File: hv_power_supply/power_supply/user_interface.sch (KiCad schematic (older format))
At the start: 28 parts, among them SW1? EMS22A50-B28-LS6

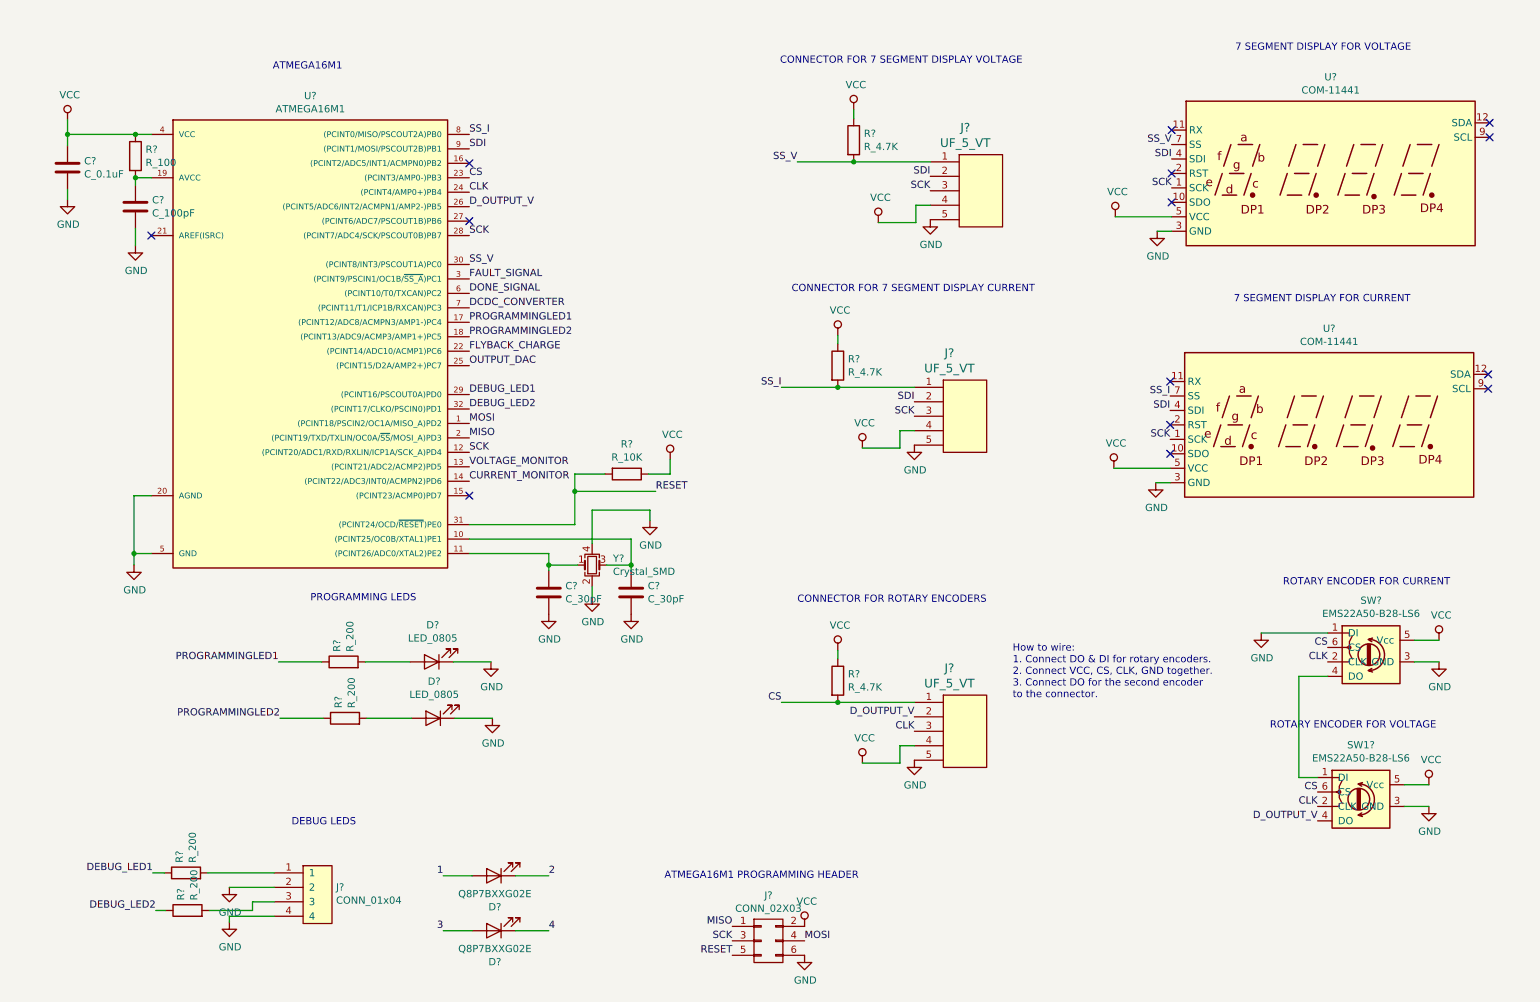
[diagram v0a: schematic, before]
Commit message: make schematic sheets talk to each other
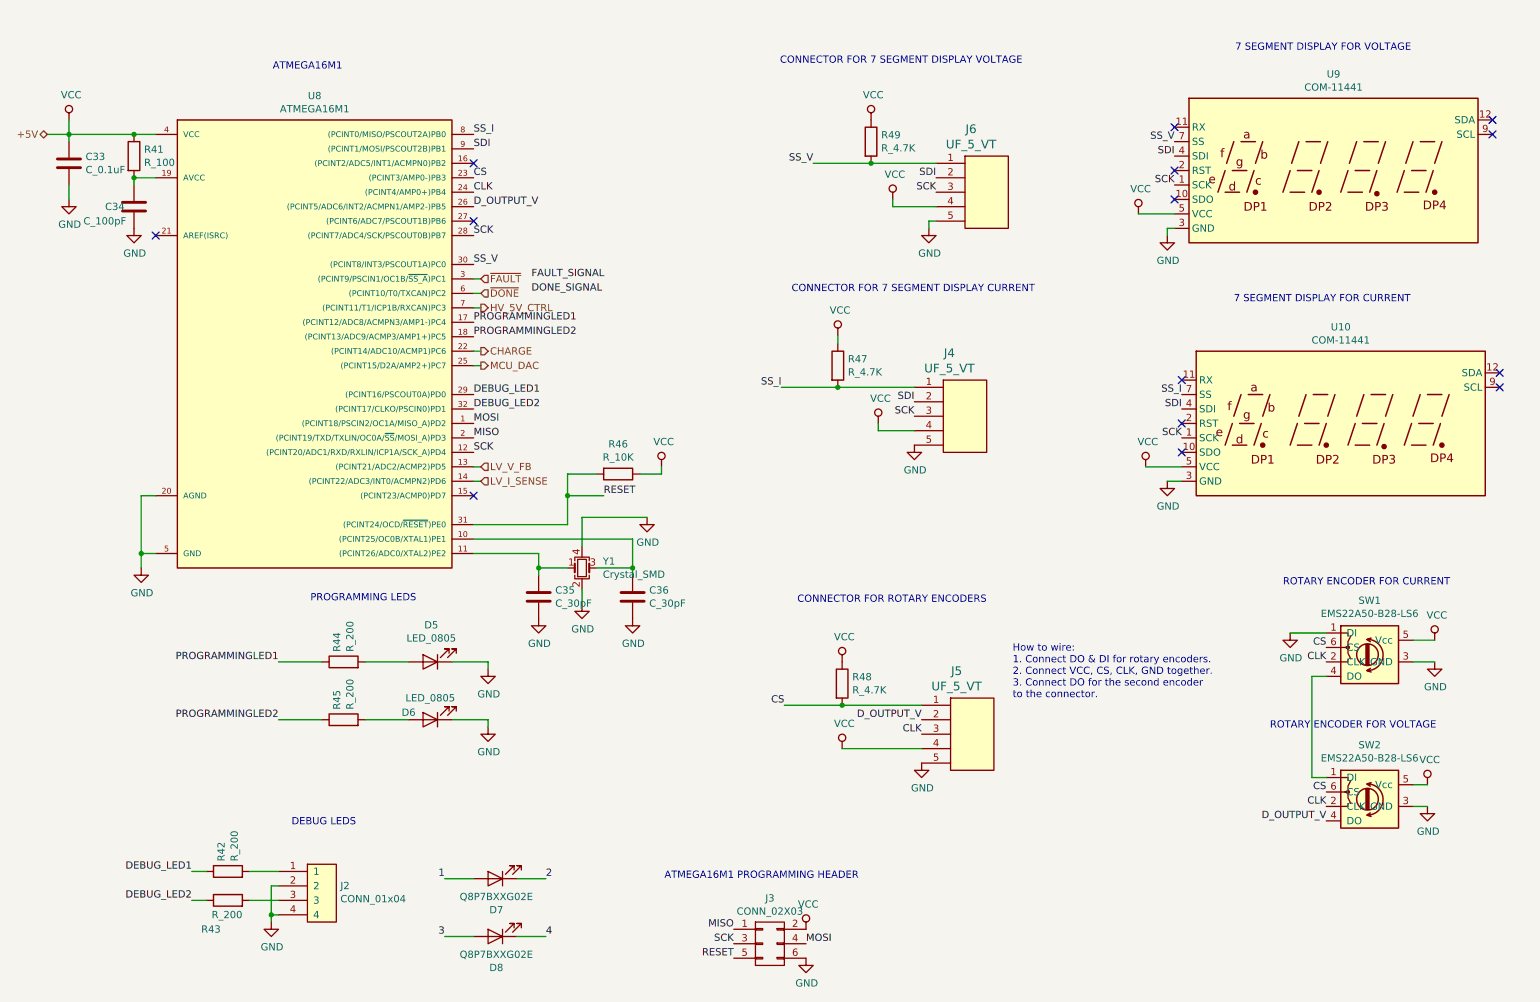
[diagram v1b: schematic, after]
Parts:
- gave numbers to parts that had none: 28
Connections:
- net DONE_SIGNAL: no longer U8.6 ((PCINT10/T0/TXCAN)PC2)
- net FAULT_SIGNAL: no longer U8.3 ((PCINT9/PSCIN1/OC1B/~SS_A~)PC1)
- net CURRENT_MONITOR renamed LV_I_SENSE
- net DCDC_CONVERTER renamed HV_5V_CTRL
- net FLYBACK_CHARGE renamed CHARGE
- net OUTPUT_DAC renamed MCU_DAC
- net VOLTAGE_MONITOR renamed LV_V_FB
- new net ~DONE: U8.6 ((PCINT10/T0/TXCAN)PC2)
- new net ~FAULT: U8.3 ((PCINT9/PSCIN1/OC1B/~SS_A~)PC1)
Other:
- moved on the sheet: C33, C35, C36, D6, D7, D8, J2, J3, J5, J6, R42, R43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

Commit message: removed footprints from off-board components
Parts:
- D7, D8: footprint footprints:LED_0805_OEM -> (none)
- U10, U9: footprint Display_7Segment:CA56-12EWA -> (none)
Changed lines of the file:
@@
 F 0 "U9" H 9650 2417 50  0000 C CNN
 F 1 "COM-11441" H 9650 2326 50  0000 C CNN
-F 2 "Display_7Segment:CA56-12EWA" H 9650 1150 50  0001 C CNN
+F 2 "" H 9650 1150 50  0001 C CNN
 F 3 "https://github.com/sparkfun/Serial7SegmentDisplay/wiki/Serial-7-Segment-Display-Datasheet" H 9220 1780 50  0001 C CNN
 	1    9650 1750
@@
 F 0 "D7" H 3843 6866 50  0000 C CNN
 F 1 "Q8P7BXXG02E" H 3843 6775 50  0000 C CNN
-F 2 "footprints:LED_0805_OEM" H 3750 6650 50  0001 C CNN
+F 2 "" H 3750 6650 50  0001 C CNN
 F 3 "https://www.apem.com/us/index.php?controller=attachment&id_attachment=1780" H 3850 6750 50  0001 C CNN
 F 4 "DK" H 3850 6650 60  0001 C CNN "MFN"
@@
 F 0 "D8" H 3843 7266 50  0000 C CNN
 F 1 "Q8P7BXXG02E" H 3843 7175 50  0000 C CNN
-F 2 "footprints:LED_0805_OEM" H 3750 7050 50  0001 C CNN
+F 2 "" H 3750 7050 50  0001 C CNN
 F 3 "https://www.apem.com/us/index.php?controller=attachment&id_attachment=1780" H 3850 7150 50  0001 C CNN
 F 4 "DK" H 3850 7050 60  0001 C CNN "MFN"
@@
 F 0 "U10" H 9700 4167 50  0000 C CNN
 F 1 "COM-11441" H 9700 4076 50  0000 C CNN
-F 2 "Display_7Segment:CA56-12EWA" H 9700 2900 50  0001 C CNN
+F 2 "" H 9700 2900 50  0001 C CNN
 F 3 "https://github.com/sparkfun/Serial7SegmentDisplay/wiki/Serial-7-Segment-Display-Datasheet" H 9270 3530 50  0001 C CNN
 	1    9700 3500

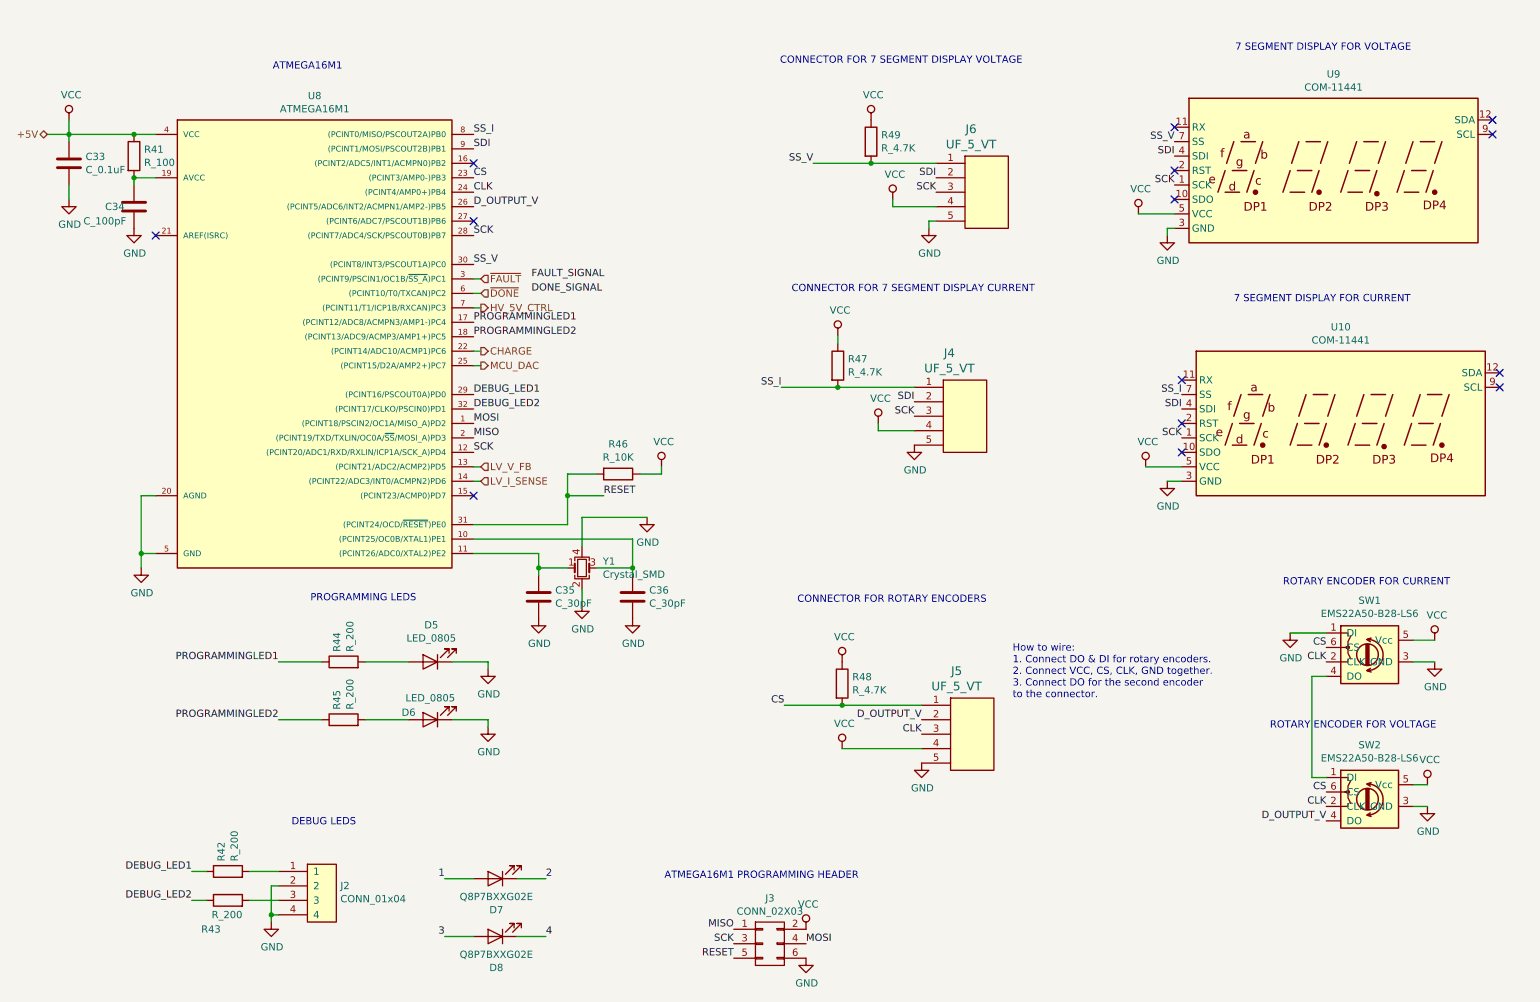
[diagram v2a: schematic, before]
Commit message: updated MCU pins
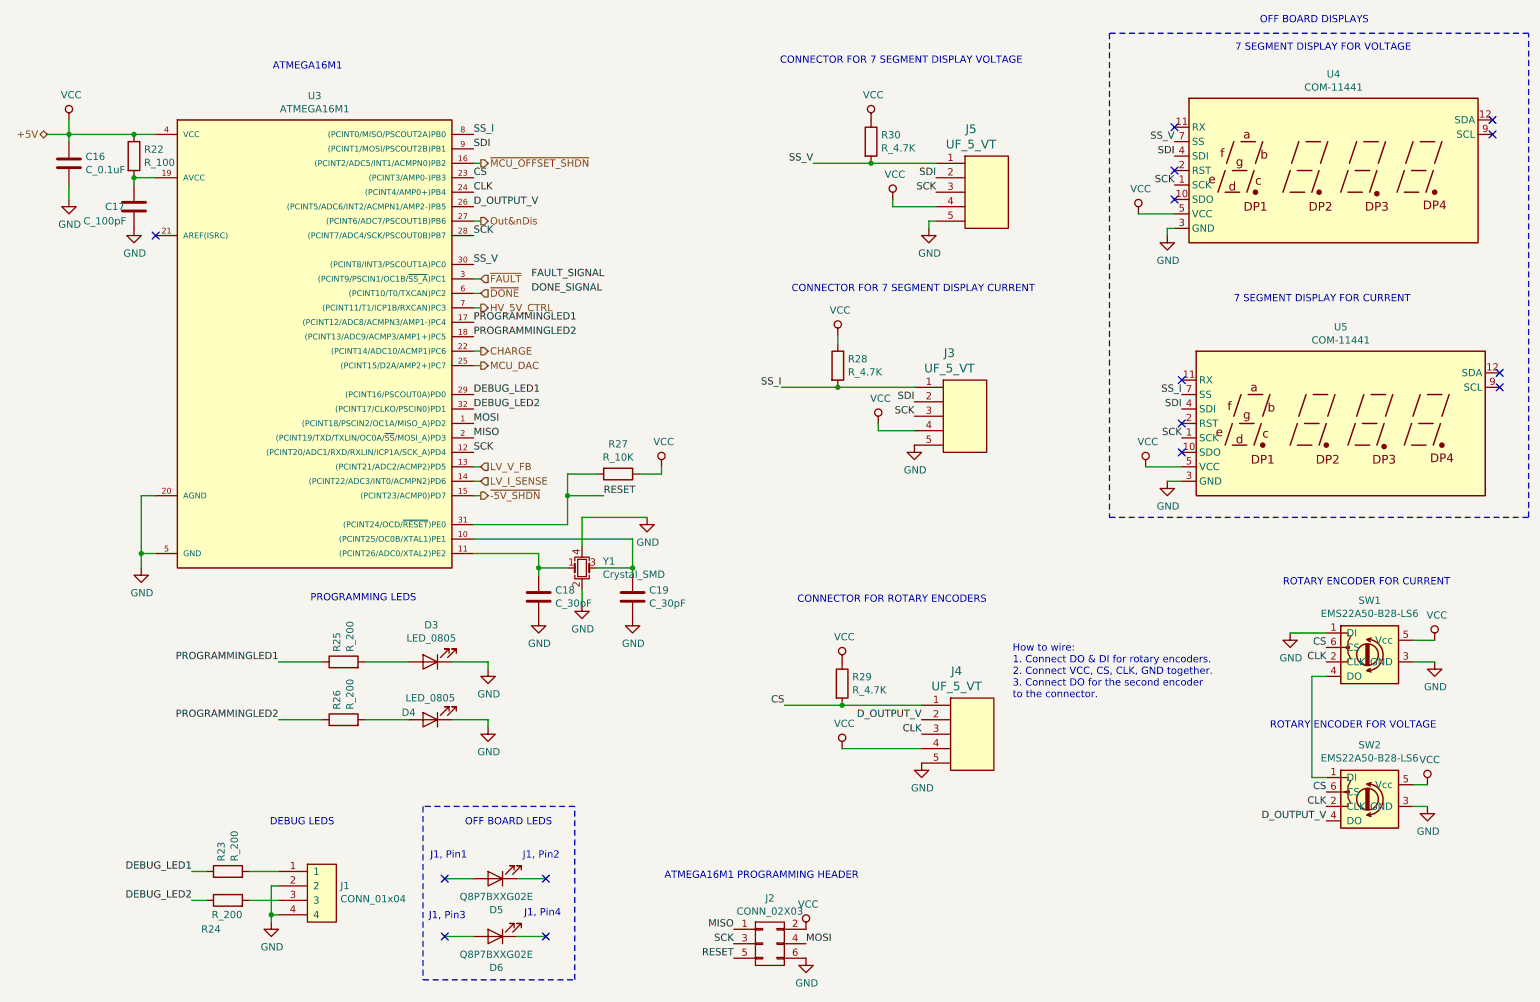
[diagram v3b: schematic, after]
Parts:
- renumbered C33 to C16, C34 to C17, C35 to C18, C36 to C19, D5 to D3, D6 to D4, D7 to D5, D8 to D6, J2 to J1, J3 to J2, J4 to J3, J5 to J4, J6 to J5, R41 to R22, R42 to R23, R43 to R24, R44 to R25, R45 to R26, R46 to R27, R47 to R28, R48 to R29, R49 to R30, U8 to U3, U9 to U4, U10 to U5
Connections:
- net ~-5V_SHDN: now reaches U3.15 ((PCINT23/ACMP0)PD7)
- net ~MCU_OFFSET_SHDN: now reaches U3.16 ((PCINT2/ADC5/INT1/ACMPN0)PB2)
- net Out&nDis: now reaches U3.27 ((PCINT6/ADC7/PSCOUT1B)PB6)
- net 1: no longer names the net of D5.2 (A)
- net 2: no longer names the net of D5.1 (K)
- net 3: no longer names the net of D6.2 (A)
- net 4: no longer names the net of D6.1 (K)
- no-connect marks 14 -> 15
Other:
- note added: "J1, Pin1\n\n"
- note added: "J1, Pin2\n"
- note added: "J1, Pin3\n\n"
- note added: "J1, Pin4\n\n"
- note added: "OFF BOARD DISPLAYS\n\n"
- note added: "OFF BOARD LEDS\n\n"

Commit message: Fixed all component footprint issues, beginning to lay out flyback portion
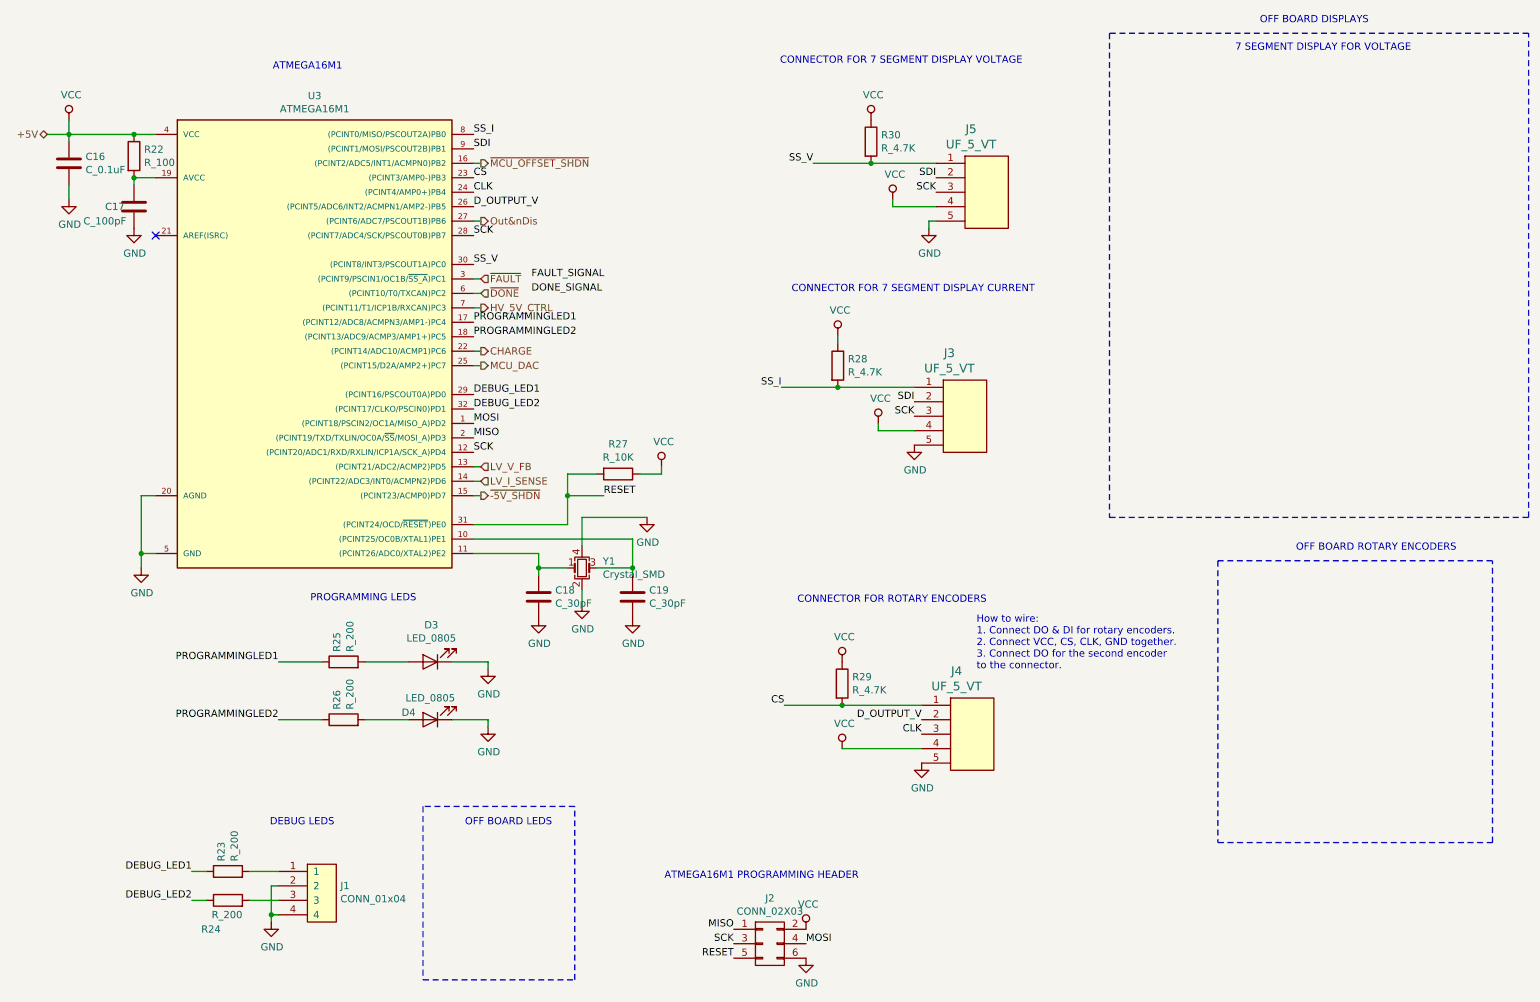
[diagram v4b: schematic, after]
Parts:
- removed D5, D6: Q8P7BXXG02E, symbol formula:Q8P7BXXG02E
- removed SW1, SW2: EMS22A50-B28-LS6, symbol formula:EMS22A50-B28-LS6
- removed U4, U5: COM-11441, symbol formula:COM-11441
- J3, J4, J5: footprint (none) -> formula:Ultrafit_5
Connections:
- no-connect marks 15 -> 1
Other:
- note added: "OFF BOARD ROTARY ENCODERS\n\n"
- note removed: "7 SEGMENT DISPLAY FOR CURRENT\n"
- note removed: "J1, Pin1\n\n"
- note removed: "J1, Pin2\n"
- note removed: "J1, Pin3\n\n"
- note removed: "J1, Pin4\n\n"
- note removed: "ROTARY ENCODER FOR CURRENT\n\n"
- note removed: "ROTARY ENCODER FOR VOLTAGE\n"
